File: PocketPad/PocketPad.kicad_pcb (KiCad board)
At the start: 2 copper layers, 72.9 x 63 mm, 43 parts, among them SW0 SW_Push, SW1 SW_Push, SW10 SW_Push, SW11 SW_Push, SW12 SW_Push, SW13 SW_Push, SW14 SW_Push, SW15 SW_Push, SW16 SW_Push, SW17 SW_Push, SW18 SW_Push, SW2 SW_Push, SW3 SW_Push, SW4 SW_Push, SW5 SW_Push, SW6 SW_Push, SW7 SW_Push, SW8 SW_Push, SW9 SW_Push

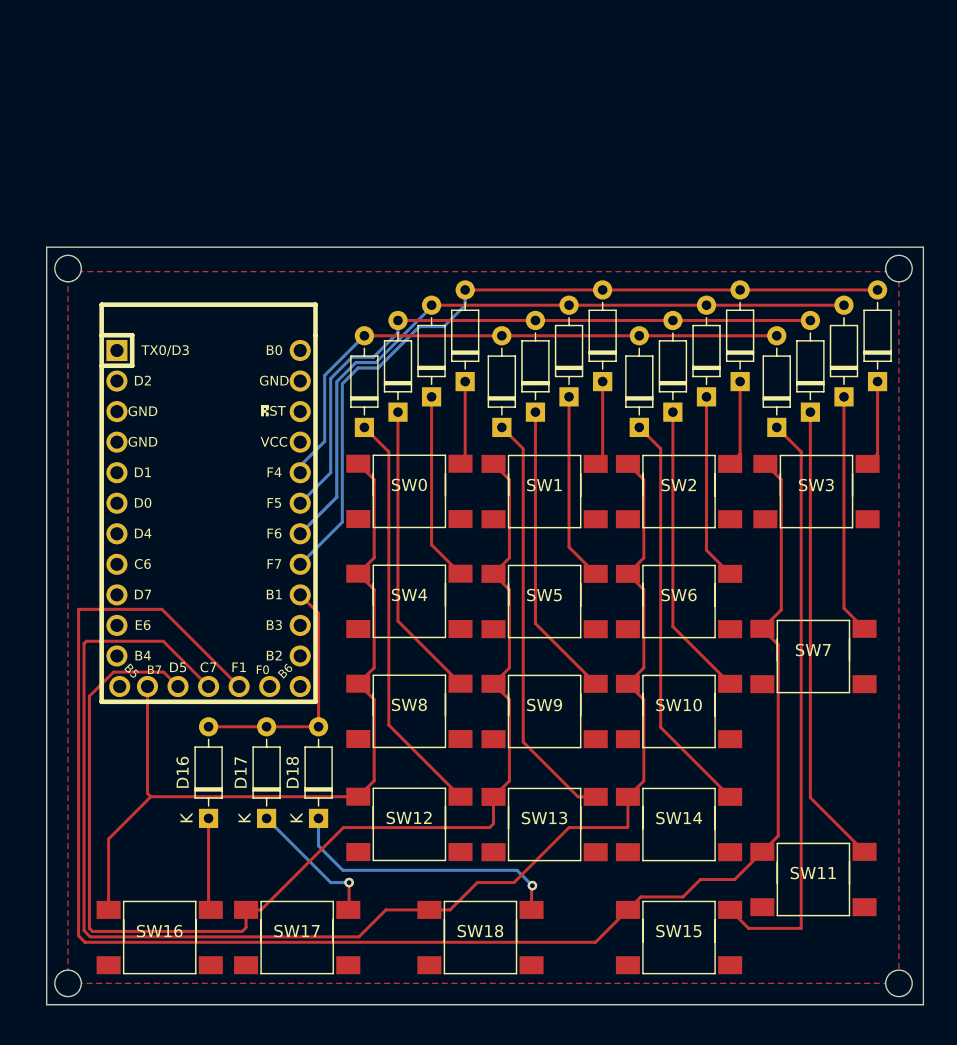
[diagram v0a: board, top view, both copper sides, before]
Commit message: Moved Mounting Holes
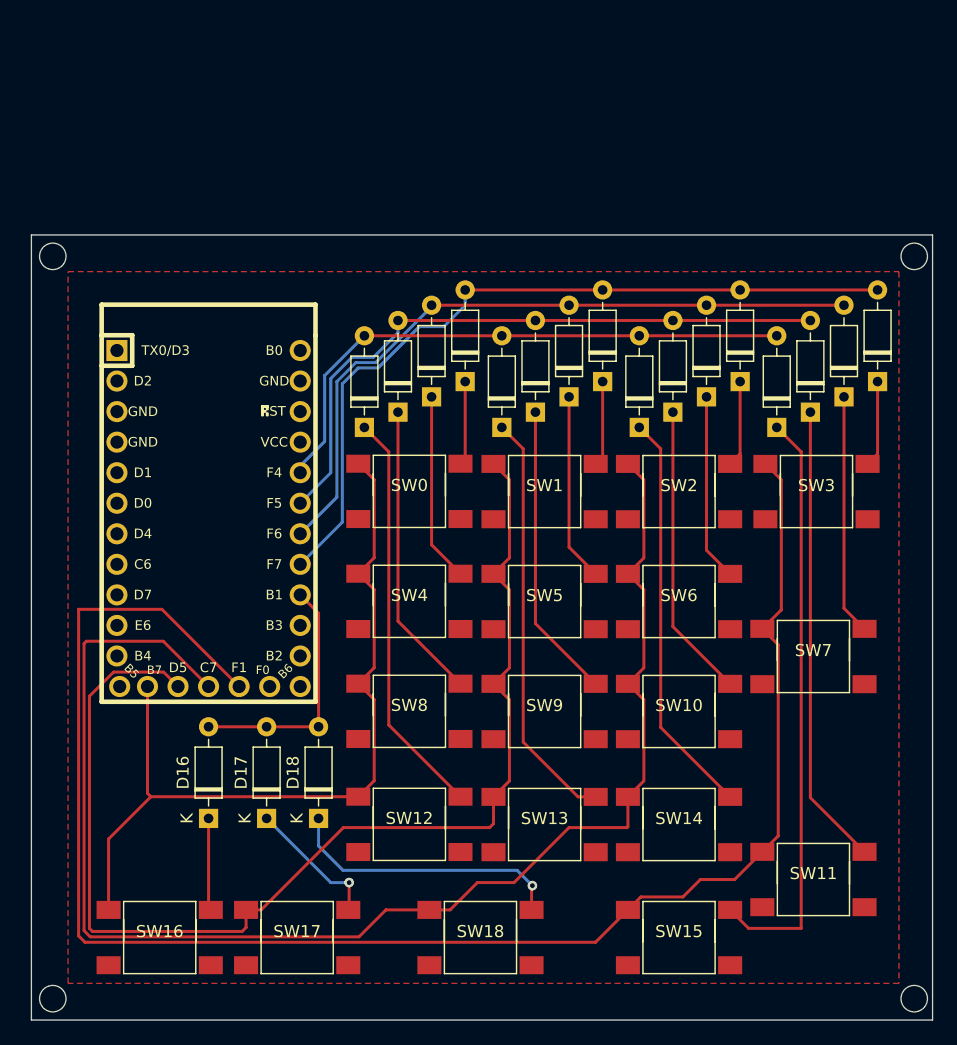
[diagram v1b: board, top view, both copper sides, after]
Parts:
- moved REF** 1.80 mm to (24.4, 97.5)
- moved REF** 1.80 mm to (96.0, 97.5)
- moved REF** 1.63 mm to (24.4, 35.8)
- moved REF** 1.63 mm to (96.0, 35.8)
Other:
- board size 72.9 x 63 mm -> 74.9 x 65.3 mm
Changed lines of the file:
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@@
   )
   (footprint "MountingHole:MountingHole_2.2mm_M2" (layer "F.Cu")
-    (at 25.654 96.266)
+    (at 24.384 97.536)
     (descr "Mounting Hole 2.2mm, no annular, M2")
     (tags "mounting hole 2.2mm no annular m2")
@@
   )
   (footprint "MountingHole:MountingHole_2.2mm_M2" (layer "F.Cu")
-    (at 94.742 36.83)
+    (at 96.012 35.814)
     (descr "Mounting Hole 2.2mm, no annular, M2")
     (tags "mounting hole 2.2mm no annular m2")
@@
   )
   (footprint "MountingHole:MountingHole_2.2mm_M2" (layer "F.Cu")
-    (at 25.654 36.83)
+    (at 24.384 35.814)
     (descr "Mounting Hole 2.2mm, no annular, M2")
     (tags "mounting hole 2.2mm no annular m2")
@@
   )
   (footprint "MountingHole:MountingHole_2.2mm_M2" (layer "F.Cu")
-    (at 94.742 96.266)
+    (at 96.012 97.536)
     (descr "Mounting Hole 2.2mm, no annular, M2")
     (tags "mounting hole 2.2mm no annular m2")
@@
     )
   )
-  (gr_rect (start 23.876 35.052) (end 96.774 98.044) (layer "Edge.Cuts") (width 0.1) (fill none))
+  (gr_rect (start 22.606 34.036) (end 97.536 99.314) (layer "Edge.Cuts") (width 0.1) (fill none))
   (segment (start 49.022 87.884) (end 49.022 90.088) (width 0.25) (layer "F.Cu") (net 3))
   (segment (start 49.022 90.088) (end 48.954 90.156) (width 0.25) (layer "F.Cu") (net 3))

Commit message: edgecut replaced. Gerbers added
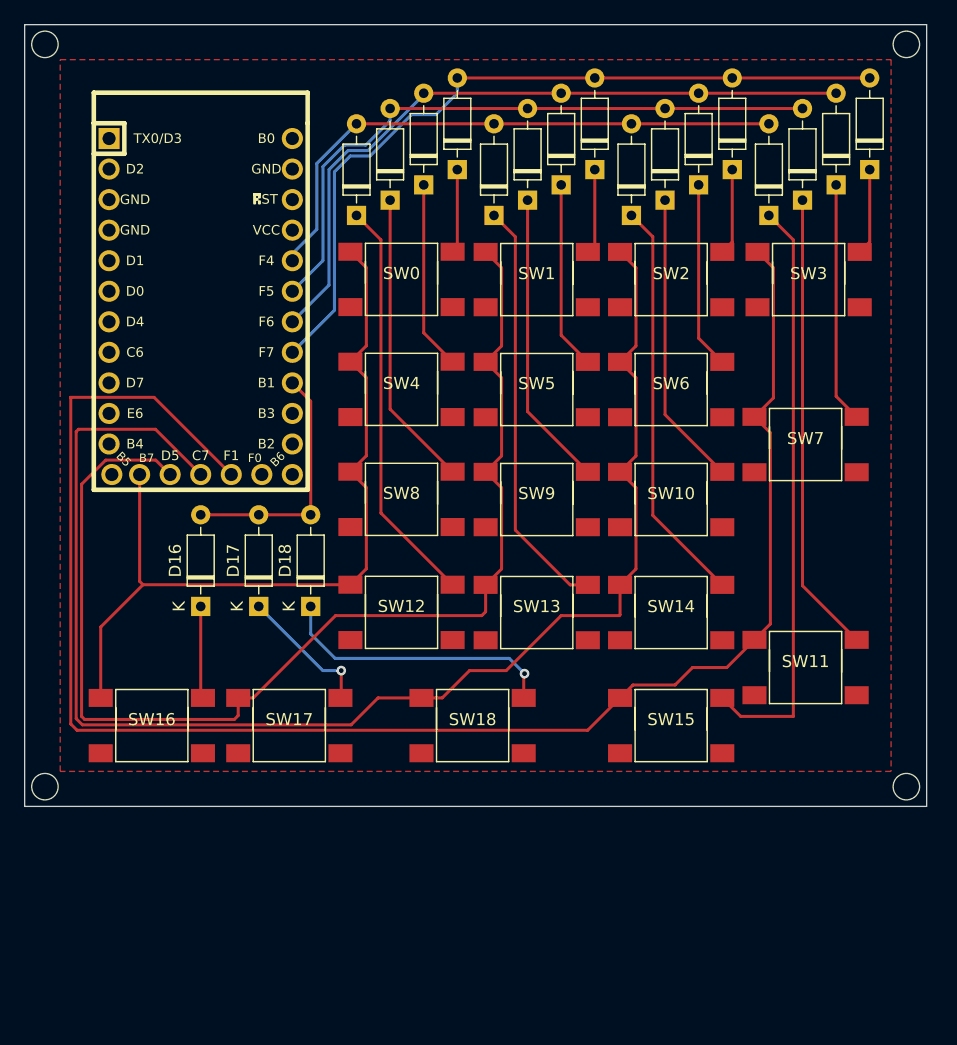
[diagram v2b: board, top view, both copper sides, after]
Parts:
- moved REF** 17.6 mm to (23.7, 79.9)
- moved REF** 17.6 mm to (95.4, 79.9)
- moved SW13 17.6 mm to (64.6, 65.4)
- moved SW14 17.6 mm to (75.8, 65.4)
- moved SW15 17.6 mm to (75.8, 74.8)
- moved SW16 17.6 mm to (32.6, 74.8)
- moved SW17 17.6 mm to (44.0, 74.8)
- moved SW18 17.6 mm to (59.3, 74.8)
- moved SW5 17.6 mm to (64.6, 46.9)
- moved SW6 17.6 mm to (75.8, 46.9)
- moved D0 17.6 mm to (58.0, 28.6)
- moved D1 17.6 mm to (69.5, 28.6)
- moved D10 17.6 mm to (75.3, 31.1)
- moved D11 17.6 mm to (86.7, 31.1)
- moved D2 17.6 mm to (80.9, 28.6)
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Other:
- board size 74.9 x 65.3 mm -> 75 x 65 mm

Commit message: Replaced Footprints and THT 3D Model
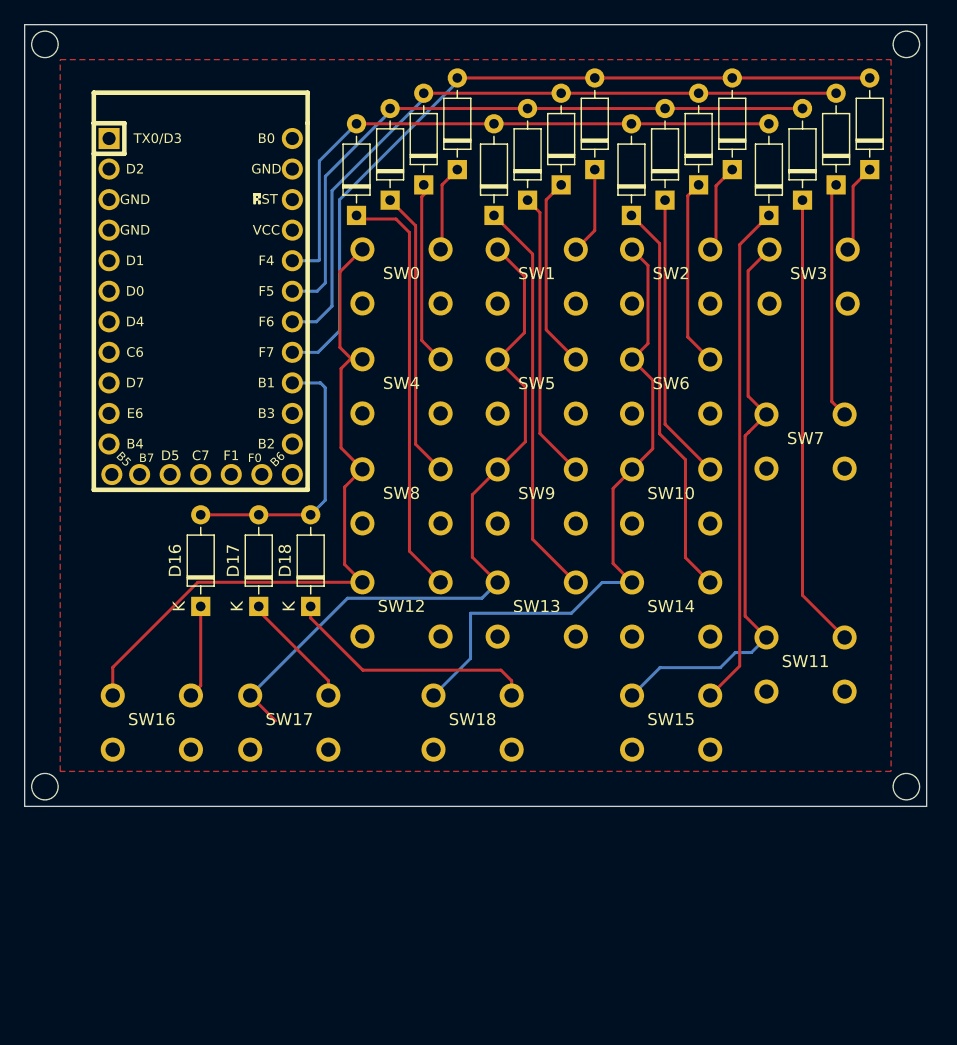
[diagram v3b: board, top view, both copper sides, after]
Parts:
- SW0, SW1, SW10, SW11, SW12, SW13, SW14, SW15, SW16, SW17, SW18, SW2, SW3, SW4, SW5, SW6, SW7, SW8, SW9: footprint Keebio:Switch_6x6x8.5 -> Keebio:Switch_THT_6x6x8.5
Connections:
- MCU1 pad 27: COL2 -> COL3
- MCU1 pad 28: COL3 -> COL2
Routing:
- net COL3: track 137.9 -> 48.3 mm
- net COL2: track 118.6 -> 54.1 mm
- net COL1: track 99.5 -> 60.7 mm
- net COL0: track 68.4 -> 59.1 mm
- net Net-(D15-Pad1): track 49.0 -> 41.9 mm
- net Net-(D18-Pad1): track 23.5 -> 21.1 mm, vias 1 -> 0
- net ROW4: track 20.7 -> 23.1 mm
- net Net-(D17-Pad1): track 11.4 -> 9.80 mm, vias 1 -> 0
- net Net-(D13-Pad1): track 34.8 -> 33.3 mm
- net ROW3: track 47.9 -> 49.2 mm
- net Net-(D12-Pad1): track 34.0 -> 35.2 mm
- net Net-(D4-Pad1): track 15.7 -> 14.6 mm
- net ROW0: track 64.7 -> 64.0 mm
- net Net-(D9-Pad1): track 24.7 -> 24.1 mm
- net Net-(D8-Pad1): track 24.7 -> 24.1 mm
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
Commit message: Readded models and replaced footprint. Silkscreen done
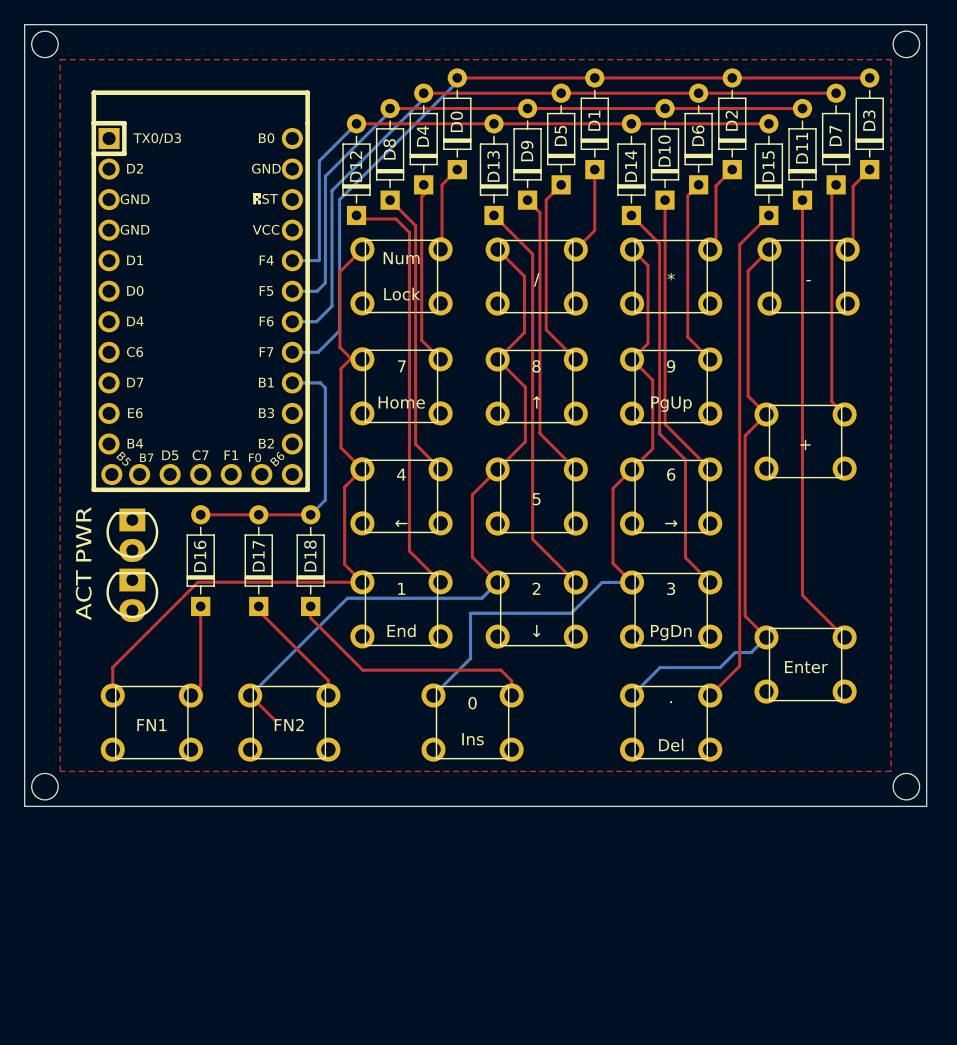
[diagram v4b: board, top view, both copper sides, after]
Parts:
- added ACT: LED, Keebio:LED_3mm, F.Cu at (31.0, 64.0)
- added PWR: LED, Keebio:LED_3mm, F.Cu at (31.0, 59.0)
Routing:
- net Net-(D1-Pad1): track 7.30 -> 68.0 mm
- net Net-(D6-Pad1): track 15.7 -> 69.8 mm
- net Net-(D3-Pad1): track 7.40 -> 55.7 mm
- net COL1: track 60.7 -> 25.9 mm
- net COL3: track 48.3 -> 19.7 mm
- net Net-(D8-Pad1): track 24.1 -> 0.00 mm
- net Net-(D10-Pad1): track 23.9 -> 0.00 mm
- net Net-(D12-Pad1): track 35.2 -> 59.1 mm
- net Net-(D18-Pad1): track 21.1 -> 0.00 mm
- net Net-(D7-Pad1): track 19.7 -> 0.00 mm
- net Net-(D5-Pad1): track 16.1 -> 0.00 mm
- net Net-(D17-Pad1): track 9.80 -> 0.00 mm
- net Net-(D2-Pad1): track 7.40 -> 0.00 mm
- net COL2: track 54.1 -> 52.4 mm

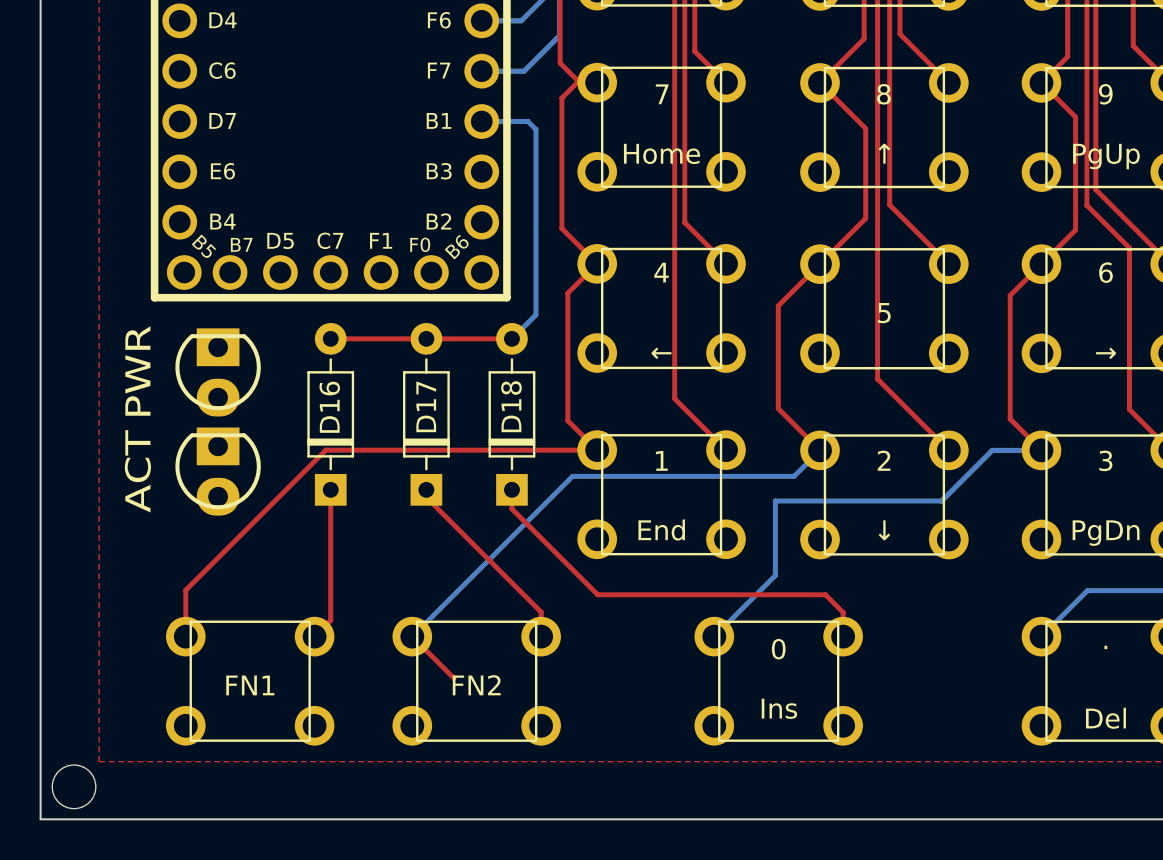
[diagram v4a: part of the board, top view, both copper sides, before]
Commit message: V0.2 : Removed SW18
Redid trace routes. Removed SW18, moved SW16,17 over. Moved PWR & ACT LEDs
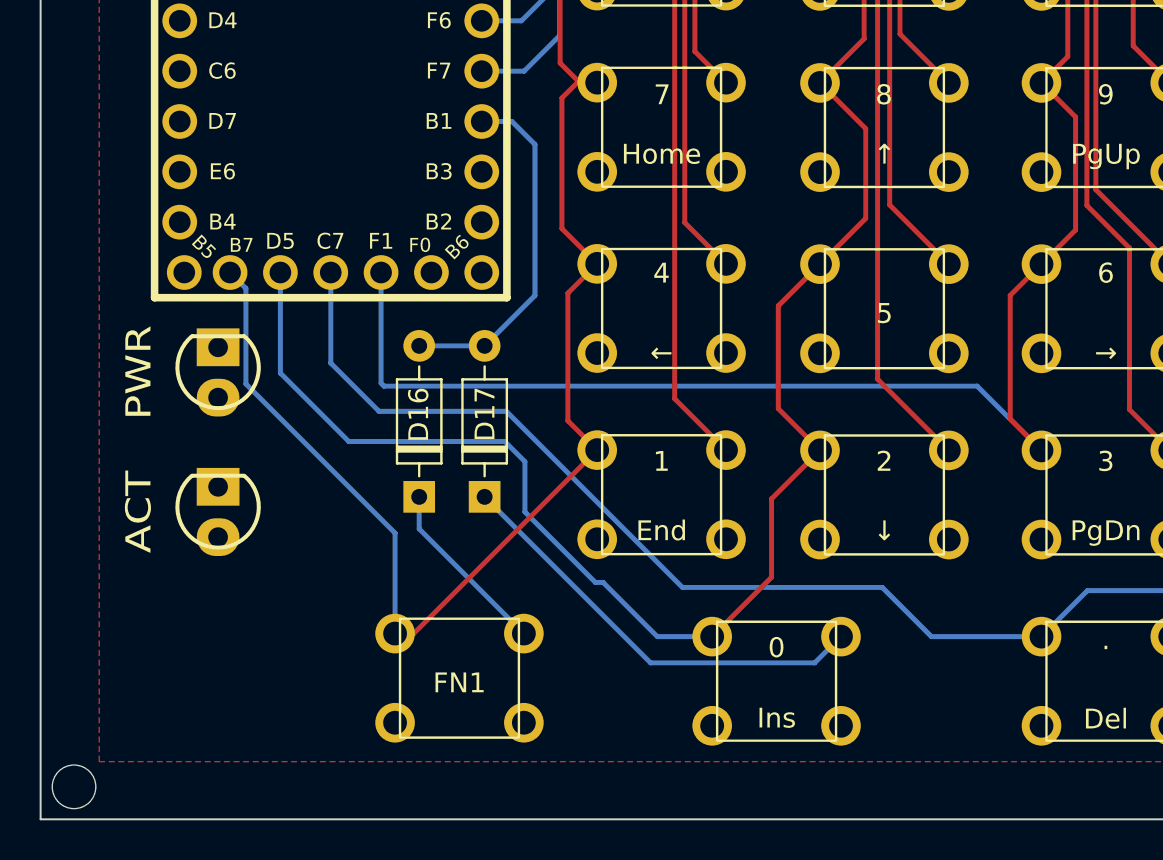
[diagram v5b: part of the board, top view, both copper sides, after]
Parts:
- removed D18: DIODE, Diode_THT:D_DO-35_SOD27_P7.62mm_Horizontal
- removed SW18: SW_Push, Keebio:Switch_THT_6x6x8.5
- moved SW17 15.1 mm to (59.2, 74.8)
- moved SW16 10.6 mm to (43.2, 74.7)
- moved D16 4.48 mm to (41.1, 65.3)
- moved D17 2.96 mm to (44.5, 65.3)
- moved ACT 2.04 mm to (31.0, 66.0)
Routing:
- net COL3: track 19.7 -> 94.4 mm
- net Net-(D1-Pad1): track 68.0 -> 7.30 mm
- net Net-(D6-Pad1): track 69.8 -> 15.7 mm
- net COL1: track 25.9 -> 78.7 mm
- net Net-(D3-Pad1): track 55.7 -> 7.40 mm
- net Net-(D8-Pad1): track 0.00 -> 24.1 mm
- net Net-(D10-Pad1): track 0.00 -> 23.9 mm
- net Net-(D12-Pad1): track 59.1 -> 35.2 mm
- net Net-(D17-Pad1): track 0.00 -> 22.0 mm
- net Net-(D7-Pad1): track 0.00 -> 19.7 mm
- net COL2: track 52.4 -> 71.8 mm
- net Net-(D5-Pad1): track 0.00 -> 16.1 mm
- net COL0: track 59.3 -> 68.7 mm
- net Net-(D2-Pad1): track 0.00 -> 7.40 mm
- net ROW4: track 23.1 -> 17.7 mm
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
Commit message: ....
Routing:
- net COL0: track 68.7 -> 70.2 mm
- net COL1: track 78.7 -> 77.4 mm
- net COL3: track 94.4 -> 93.9 mm
